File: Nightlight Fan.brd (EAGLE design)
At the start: 51.1 x 59.7 mm, 17 parts, among them J2 USB_A_SMT_MALE_HOLE_MOUNT, Q1 2N3904, U1 ATMEGA328, X1 53048-ROUND-02

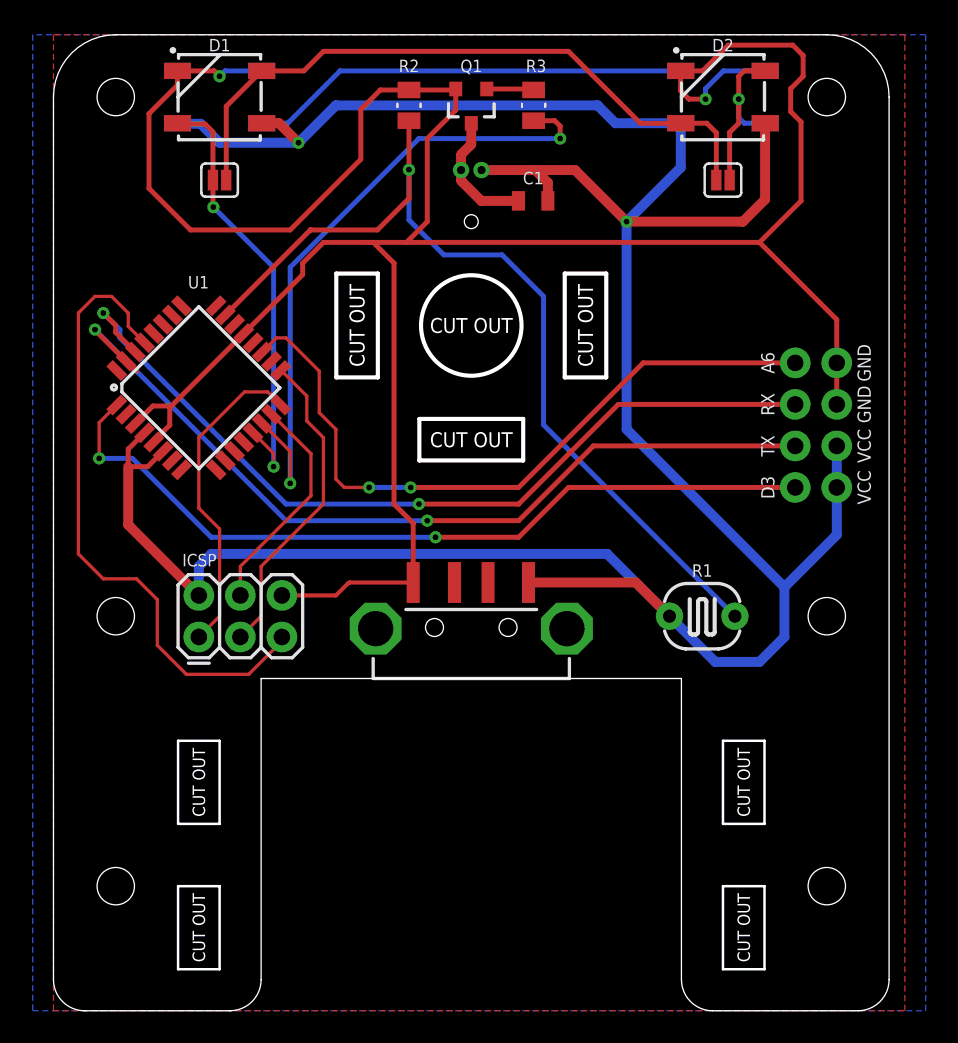
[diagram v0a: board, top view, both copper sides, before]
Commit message: v1.01 - Moved USB port slightly beyond PCB edge, increased motor wire relief hole size
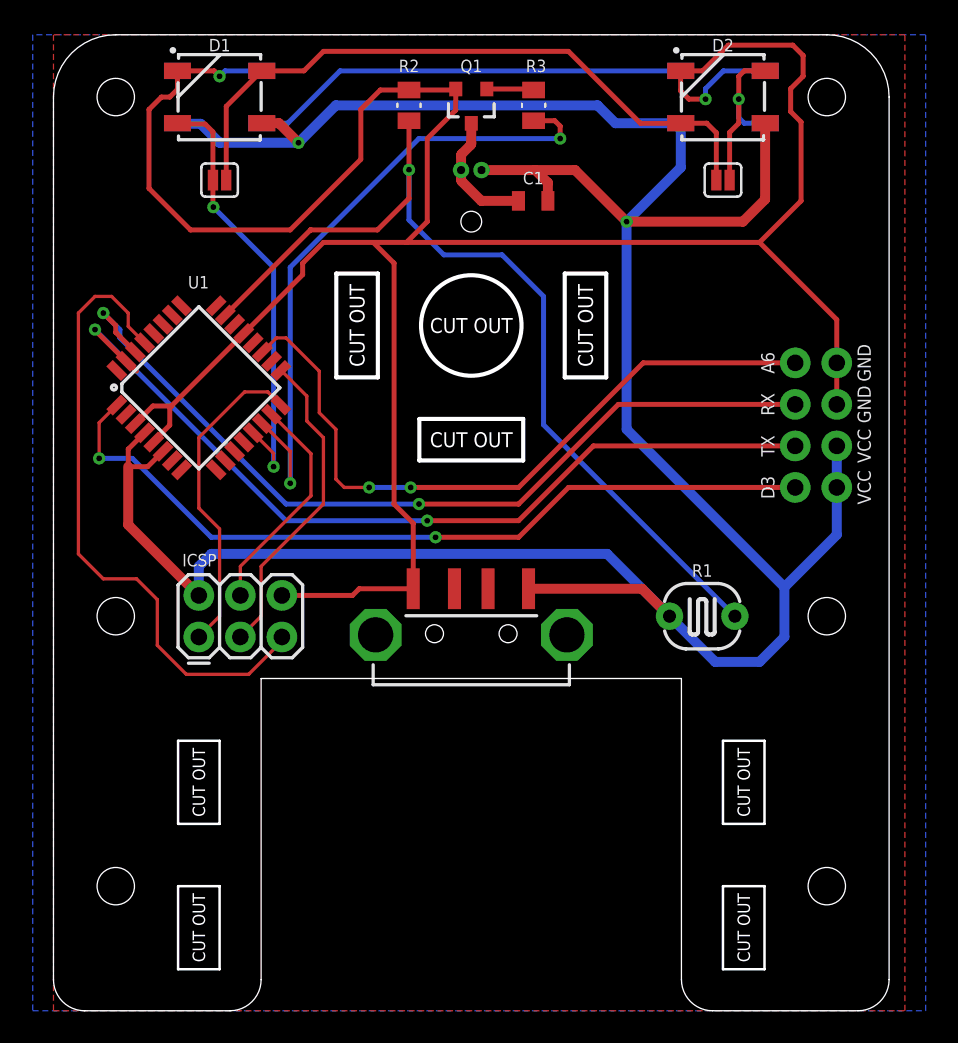
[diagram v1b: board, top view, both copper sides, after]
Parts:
- moved J2 0.38 mm to (25.6, 14.9)
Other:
- board text added: "Ben Perkins - 1/3/2017"
- board text added: "Nightlight & towel dryer - v1.01"
- board text removed: "Ben Perkins - 12/7/2017"
- board text removed: "Nightlight & towel dryer - v1.0"
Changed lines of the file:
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@@
 <?xml version="1.0" encoding="utf-8"?>
 <!DOCTYPE eagle SYSTEM "eagle.dtd">
-<eagle version="8.4.3">
+<eagle version="8.5.1">
 <drawing>
 <settings>
-<setting alwaysvectorfont="yes"/>
+<setting alwaysvectorfont="no"/>
 <setting verticaltext="up"/>
 </settings>
@@
 <hole x="47.2948" y="24.13" drill="2.286"/>
 <hole x="47.2948" y="7.62" drill="2.286"/>
-<hole x="25.5524" y="48.26" drill="0.85"/>
+<hole x="25.5524" y="48.26" drill="1.27"/>
 <circle x="25.5524" y="41.91" radius="16.51" width="0.1524" layer="48"/>
 <circle x="39.37" y="46.736" radius="1.778" width="0.6096" layer="30"/>
@@
 <text x="42.2148" y="5.08" size="0.762" layer="20" ratio="10" rot="R90" align="center">CUT OUT</text>
 <text x="42.2148" y="13.97" size="0.762" layer="20" ratio="10" rot="R90" align="center">CUT OUT</text>
-<text x="6.223" y="40.005" size="1.016" layer="22" font="vector" ratio="12" rot="SMR270" align="center">Nightlight &amp; towel dryer - v1.0</text>
-<text x="8.128" y="40.005" size="1.016" layer="22" font="vector" ratio="12" rot="SMR270" align="center">Ben Perkins - 12/7/2017</text>
+<text x="6.223" y="40.005" size="1.016" layer="22" font="vector" ratio="12" rot="SMR270" align="center">Nightlight &amp; towel dryer - v1.01</text>
+<text x="8.128" y="40.005" size="1.016" layer="22" font="vector" ratio="12" rot="SMR270" align="center">Ben Perkins - 1/3/2017</text>
 <wire x1="31.2674" y1="45.085" x2="33.8074" y2="45.085" width="0.254" layer="20"/>
 <wire x1="33.8074" y1="45.085" x2="33.8074" y2="38.735" width="0.254" layer="20"/>
@@
 <param name="srMinRoundness" value="0mil"/>
 <param name="srMaxRoundness" value="0mil"/>
-<param name="slThermalIsolate" value="10mil"/>
+<param name="slThermalIsolate" value="25mil"/>
 <param name="slThermalsForVias" value="0"/>
 <param name="dpMaxLengthDifference" value="10mm"/>
@@
 <param name="checkRestrict" value="1"/>
 <param name="checkStop" value="0"/>
+<param name="checkValues" value="0"/>
 <param name="useDiameter" value="13"/>
 <param name="maxErrors" value="50"/>
@@
 <attribute name="PROD_ID" value="CONN-09701" x="8.89" y="22.86" size="1.778" layer="27" display="off"/>
 </element>
-<element name="J2" library="!CustomParts" package="USB_A_SMT_MALE" value="USB_A_SMT_MALE_HOLE_MOUNT" x="25.5524" y="15.24" smashed="yes" rot="R90"/>
+<element name="J2" library="!CustomParts" package="USB_A_SMT_MALE" value="USB_A_SMT_MALE_HOLE_MOUNT" x="25.5524" y="14.859" smashed="yes" rot="R90"/>
 <element name="R1" library="SparkFun-Sensors" package="PHOTOCELL" value="PHOTOCELL" x="39.6748" y="24.13" smashed="yes">
 <attribute name="NAME" x="39.6748" y="26.543" size="0.762" layer="25" font="vector" ratio="12" align="bottom-center"/>
@@
 <wire x1="24.3898" y1="56.3118" x2="21.7424" y2="56.3118" width="0.3048" layer="1"/>
 <wire x1="24.3898" y1="56.3118" x2="24.6024" y2="56.372" width="0.3048" layer="1"/>
-<wire x1="7.583" y1="57.48" x2="7.583" y2="56.605" width="0.3048" layer="1"/>
-<wire x1="7.583" y1="56.605" x2="5.842" y2="54.864" width="0.3048" layer="1"/>
-<wire x1="5.842" y1="54.864" x2="5.842" y2="50.292" width="0.3048" layer="1"/>
 <wire x1="5.842" y1="50.292" x2="8.382" y2="47.752" width="0.3048" layer="1"/>
 <wire x1="8.382" y1="47.752" x2="14.478" y2="47.752" width="0.3048" layer="1"/>
@@
 <wire x1="15.24" y1="45.0156875" x2="15.24" y2="45.72" width="0.3048" layer="1"/>
 <wire x1="15.24" y1="45.72" x2="16.51" y2="46.99" width="0.3048" layer="1"/>
-<wire x1="19.304" y1="46.99" x2="21.59" y2="46.99" width="0.3048" layer="1"/>
-<wire x1="19.304" y1="46.99" x2="16.51" y2="46.99" width="0.3048" layer="1"/>
+<wire x1="19.558" y1="46.99" x2="21.59" y2="46.99" width="0.3048" layer="1"/>
+<wire x1="19.558" y1="46.99" x2="16.51" y2="46.99" width="0.3048" layer="1"/>
 <wire x1="22.86" y1="48.26" x2="21.59" y2="46.99" width="0.3048" layer="1"/>
 <wire x1="24.6024" y1="56.372" x2="24.6024" y2="55.0824" width="0.3048" layer="1"/>
@@
 <wire x1="43.5218" y1="57.48" x2="40.97" y2="57.48" width="0.3048" layer="16"/>
 <wire x1="40.97" y1="57.48" x2="39.878" y2="56.388" width="0.3048" layer="16"/>
-<wire x1="18.125125" y1="26.19" x2="22.0016" y2="26.19" width="0.254" layer="1"/>
-<wire x1="18.125125" y1="26.19" x2="18.0173625" y2="26.1453625" width="0.254" layer="1" curve="45"/>
-<wire x1="18.0173625" y1="26.1453625" x2="17.272" y2="25.4" width="0.254" layer="1"/>
-<wire x1="17.272" y1="25.4" x2="13.97" y2="25.4" width="0.254" layer="1"/>
 <contactref element="J1" pad="2"/>
 <contactref element="J1" pad="1"/>
-<wire x1="22.0016" y1="29.8144" x2="22.0016" y2="26.19" width="0.3048" layer="1"/>
+<wire x1="22.0016" y1="29.8144" x2="22.0016" y2="25.809" width="0.3048" layer="1"/>
 <wire x1="20.828" y1="30.988" x2="20.828" y2="45.72" width="0.3048" layer="1"/>
 <wire x1="20.828" y1="30.988" x2="22.0016" y2="29.8144" width="0.3048" layer="1"/>
@@
 <wire x1="47.9044" y1="39.624" x2="47.9044" y2="37.084" width="0.3048" layer="1"/>
 <wire x1="20.828" y1="45.72" x2="19.558" y2="46.99" width="0.3048" layer="1"/>
-<wire x1="19.558" y1="46.99" x2="19.304" y2="46.99" width="0.3048" layer="1"/>
+<wire x1="7.583" y1="56.351" x2="7.112" y2="55.88" width="0.3048" layer="1"/>
+<wire x1="7.112" y1="55.88" x2="6.604" y2="55.88" width="0.3048" layer="1"/>
+<wire x1="6.604" y1="55.88" x2="5.842" y2="55.118" width="0.3048" layer="1"/>
+<wire x1="7.583" y1="57.48" x2="7.583" y2="56.351" width="0.3048" layer="1"/>
+<wire x1="5.842" y1="55.118" x2="5.842" y2="50.292" width="0.3048" layer="1"/>
+<wire x1="22.0016" y1="25.809" x2="18.697" y2="25.809" width="0.3048" layer="1"/>
+<wire x1="18.697" y1="25.809" x2="18.288" y2="25.4" width="0.3048" layer="1"/>
+<wire x1="18.288" y1="25.4" x2="13.97" y2="25.4" width="0.3048" layer="1"/>
 </signal>
 <signal name="N$1">
@@
 <contactref element="U1" pad="6"/>
 <contactref element="ICSP" pad="2"/>
-<wire x1="35.6148" y1="26.19" x2="29.0524" y2="26.19" width="0.6096" layer="1"/>
-<wire x1="35.6148" y1="26.19" x2="37.6748" y2="24.13" width="0.6096" layer="1"/>
 <contactref element="D1" pad="1"/>
 <contactref element="D2" pad="1"/>
@@
 <wire x1="30.237" y1="49.53" x2="30.237" y2="50.642" width="0.6096" layer="1"/>
 <wire x1="30.237" y1="50.642" x2="29.464" y2="51.415" width="0.6096" layer="1"/>
+<wire x1="29.0524" y1="25.809" x2="35.9958" y2="25.809" width="0.6096" layer="1"/>
+<wire x1="35.9958" y1="25.809" x2="37.6748" y2="24.13" width="0.6096" layer="1"/>
 </signal>
 <signal name="N$5">
@@
 <contactref element="R1" pad="2"/>
 <contactref element="R2" pad="2"/>
-<wire x1="41.6748" y1="24.13" x2="41.656" y2="24.1488" width="0.3048" layer="1"/>
 <via x="21.7424" y="51.435" extent="1-16" drill="0.35"/>
 <wire x1="15.7307875" y1="47.7692125" x2="10.5111125" y2="42.5495375" width="0.3048" layer="1"/>
